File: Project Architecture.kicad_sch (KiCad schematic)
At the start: 0 parts

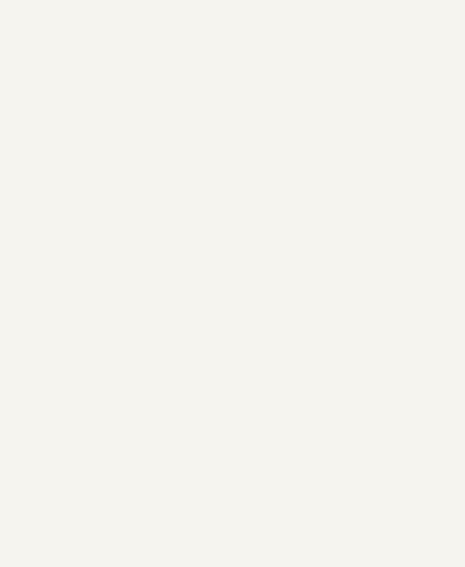
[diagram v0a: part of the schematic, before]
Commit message: dev: pull-up R901
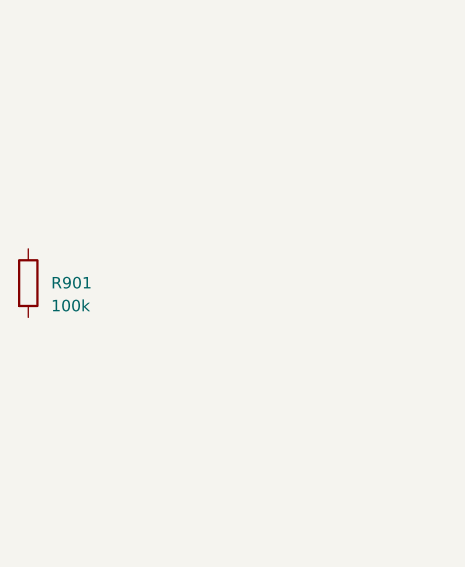
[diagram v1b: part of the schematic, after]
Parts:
- added R901: 100k, Resistor_SMD:R_0603_1608Metric, symbol Device:R
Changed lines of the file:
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@@
+		)
+	)
+	(symbol
+		(lib_id "Device:R")
+		(at 50.8 50.8 0)
+		(unit 1)
+		(exclude_from_sim no)
+		(in_bom yes)
+		(on_board yes)
+		(dnp no)
+		(property "Reference" "R901"
+			(at 53.339999999999996 50.8 0)
+			(effects (font (size 1.27 1.27)) (justify left))
+		)
+		(property "Value" "100k"
+			(at 53.339999999999996 53.339999999999996 0)
+			(effects (font (size 1.27 1.27)) (justify left))
+		)
+		(property "Footprint" "Resistor_SMD:R_0603_1608Metric"
+			(at 50.8 50.8 0)
+			(effects (font (size 1.27 1.27)) (hide yes))
+		)
+		(property "Datasheet" "~"
+			(at 50.8 50.8 0)
+			(effects (font (size 1.27 1.27)) (hide yes))
+		)
+		(pin "1")
+		(pin "2")
+		(instances
+			(project "ci_dummy"
+				(path "/f9e05184-c88b-4a88-ae9c-ab2bdb32be7c/c5103ceb-5325-4a84-a025-9638a412984e"
+					(reference "R901")
+					(unit 1)
+				)
+			)
 		)
 	)

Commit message: dev: pull-up R902
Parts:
- added R902: 100k, Resistor_SMD:R_0603_1608Metric, symbol Device:R
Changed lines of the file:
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@@
+		)
+	)
+	(symbol
+		(lib_id "Device:R")
+		(at 60.96 50.8 0)
+		(unit 1)
+		(exclude_from_sim no)
+		(in_bom yes)
+		(on_board yes)
+		(dnp no)
+		(property "Reference" "R902"
+			(at 63.5 50.8 0)
+			(effects (font (size 1.27 1.27)) (justify left))
+		)
+		(property "Value" "100k"
+			(at 63.5 53.339999999999996 0)
+			(effects (font (size 1.27 1.27)) (justify left))
+		)
+		(property "Footprint" "Resistor_SMD:R_0603_1608Metric"
+			(at 60.96 50.8 0)
+			(effects (font (size 1.27 1.27)) (hide yes))
+		)
+		(property "Datasheet" "~"
+			(at 60.96 50.8 0)
+			(effects (font (size 1.27 1.27)) (hide yes))
+		)
+		(pin "1")
+		(pin "2")
+		(instances
+			(project "ci_dummy"
+				(path "/f9e05184-c88b-4a88-ae9c-ab2bdb32be7c/c5103ceb-5325-4a84-a025-9638a412984e"
+					(reference "R902")
+					(unit 1)
+				)
+			)
 		)
 	)

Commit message: dev: R903 in parent
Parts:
- added R903: 1k, Resistor_SMD:R_0603_1608Metric, symbol Device:R
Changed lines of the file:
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@@
+		)
+	)
+	(symbol
+		(lib_id "Device:R")
+		(at 71.12 50.8 0)
+		(unit 1)
+		(exclude_from_sim no)
+		(in_bom yes)
+		(on_board yes)
+		(dnp no)
+		(property "Reference" "R903"
+			(at 73.66000000000001 50.8 0)
+			(effects (font (size 1.27 1.27)) (justify left))
+		)
+		(property "Value" "1k"
+			(at 73.66000000000001 53.339999999999996 0)
+			(effects (font (size 1.27 1.27)) (justify left))
+		)
+		(property "Footprint" "Resistor_SMD:R_0603_1608Metric"
+			(at 71.12 50.8 0)
+			(effects (font (size 1.27 1.27)) (hide yes))
+		)
+		(property "Datasheet" "~"
+			(at 71.12 50.8 0)
+			(effects (font (size 1.27 1.27)) (hide yes))
+		)
+		(pin "1")
+		(pin "2")
+		(instances
+			(project "ci_dummy"
+				(path "/f9e05184-c88b-4a88-ae9c-ab2bdb32be7c/c5103ceb-5325-4a84-a025-9638a412984e"
+					(reference "R903")
+					(unit 1)
+				)
+			)
 		)
 	)

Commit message: dev: R905
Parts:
- added R905: 10k, Resistor_SMD:R_0603_1608Metric, symbol Device:R
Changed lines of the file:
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@@
+		)
+	)
+	(symbol
+		(lib_id "Device:R")
+		(at 91.44 50.8 0)
+		(unit 1)
+		(exclude_from_sim no)
+		(in_bom yes)
+		(on_board yes)
+		(dnp no)
+		(property "Reference" "R905"
+			(at 93.98 50.8 0)
+			(effects (font (size 1.27 1.27)) (justify left))
+		)
+		(property "Value" "10k"
+			(at 93.98 53.339999999999996 0)
+			(effects (font (size 1.27 1.27)) (justify left))
+		)
+		(property "Footprint" "Resistor_SMD:R_0603_1608Metric"
+			(at 91.44 50.8 0)
+			(effects (font (size 1.27 1.27)) (hide yes))
+		)
+		(property "Datasheet" "~"
+			(at 91.44 50.8 0)
+			(effects (font (size 1.27 1.27)) (hide yes))
+		)
+		(pin "1")
+		(pin "2")
+		(instances
+			(project "ci_dummy"
+				(path "/f9e05184-c88b-4a88-ae9c-ab2bdb32be7c/c5103ceb-5325-4a84-a025-9638a412984e"
+					(reference "R905")
+					(unit 1)
+				)
+			)
 		)
 	)
